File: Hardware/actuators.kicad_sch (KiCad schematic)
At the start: 10 parts, among them J11 Conn_01x08_Socket, J14 ServoCH1, J15 ServoCH2

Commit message: Finished Boosts and Sensors
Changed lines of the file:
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@@
 (kicad_sch
-	(version 20231120)
+	(version 20250114)
 	(generator "eeschema")
-	(generator_version "8.0")
+	(generator_version "9.0")
 	(paper "A4")
 	(junction
@@
 	(label "Servo2PWM"
 		(at 88.646 88.392 90)
-		(fields_autoplaced yes)
 		(effects
 			(font
@@
 	(label "Servo1PWM"
 		(at 96.7393 87.8116 90)
-		(fields_autoplaced yes)
 		(effects
 			(font
@@
 	(label "Servo1PWM"
 		(at 98.298 47.498 90)
-		(fields_autoplaced yes)
 		(effects
 			(font
@@
 	(label "Servo1PWM"
 		(at 64.516 94.234 180)
-		(fields_autoplaced yes)
 		(effects
 			(font
@@
 	(label "Servo2PWM"
 		(at 64.516 97.282 180)
-		(fields_autoplaced yes)
 		(effects
 			(font
@@
 	(label "Servo2PWM"
 		(at 98.298 62.738 90)
-		(fields_autoplaced yes)
 		(effects
 			(font
@@
 		(shape input)
 		(at 245.618 73.406 180)
-		(fields_autoplaced yes)
 		(effects
 			(font
@@
 		(shape bidirectional)
 		(at 67.056 94.234 0)
-		(fields_autoplaced yes)
 		(effects
 			(font
@@
 		(shape input)
 		(at 245.618 78.486 180)
-		(fields_autoplaced yes)
 		(effects
 			(font
@@
 		(shape input)
 		(at 215.646 107.95 180)
-		(fields_autoplaced yes)
 		(effects
 			(font
@@
 		(shape input)
 		(at 248.412 107.95 0)
-		(fields_autoplaced yes)
 		(effects
 			(font
@@
 		(shape input)
 		(at 245.618 75.946 180)
-		(fields_autoplaced yes)
 		(effects
 			(font
@@
 		(shape output)
 		(at 137.16 106.68 180)
-		(fields_autoplaced yes)
 		(effects
 			(font
@@
 		(shape input)
 		(at 245.618 70.866 180)
-		(fields_autoplaced yes)
 		(effects
 			(font
@@
 		(shape input)
 		(at 215.646 102.87 180)
-		(fields_autoplaced yes)
 		(effects
 			(font
@@
 		(shape input)
 		(at 248.412 105.41 0)
-		(fields_autoplaced yes)
 		(effects
 			(font
@@
 		(shape input)
 		(at 248.412 102.87 0)
-		(fields_autoplaced yes)
 		(effects
 			(font
@@
 		(shape bidirectional)
 		(at 67.056 97.282 0)
-		(fields_autoplaced yes)
 		(effects
 			(font
@@
 		(shape input)
 		(at 215.646 110.49 180)
-		(fields_autoplaced yes)
-		(effects
-			(font
+		(effects
+			(font

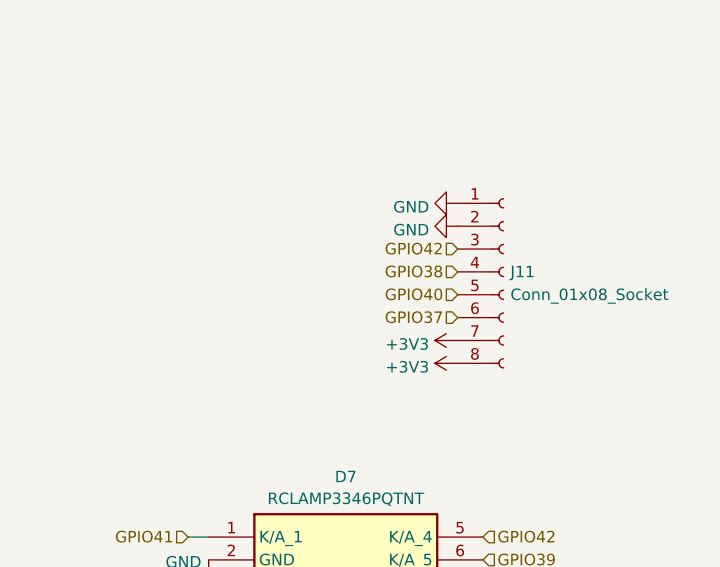
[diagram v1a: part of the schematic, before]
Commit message: Updated SD card, GPIOs, CAN, Power section
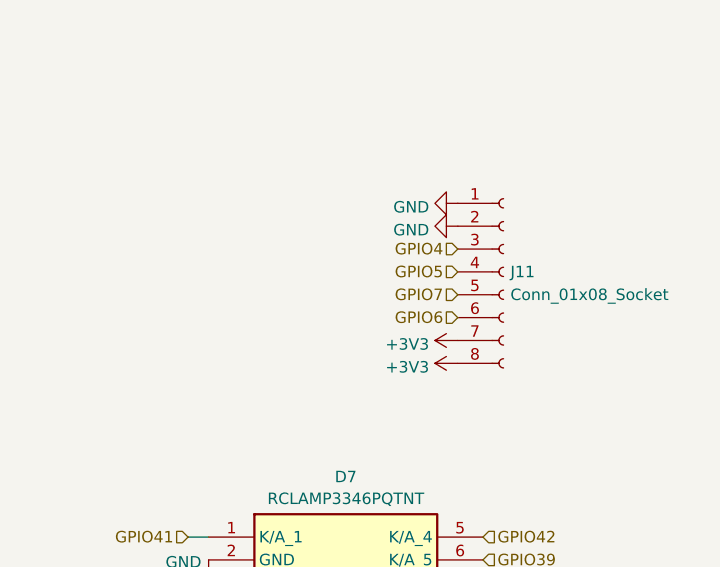
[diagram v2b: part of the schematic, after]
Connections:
- net GPIO37: no longer J11.6 (Pin_6)
- net GPIO38: no longer J11.4 (Pin_4)
- net GPIO40: no longer J11.5 (Pin_5)
- net GPIO42: no longer J11.3 (Pin_3)
- new net GPIO4: J11.3 (Pin_3)
- new net GPIO5: J11.4 (Pin_4)
- new net GPIO6: J11.6 (Pin_6)
- new net GPIO7: J11.5 (Pin_5)
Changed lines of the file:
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@@
 		)
 	)
-	(hierarchical_label "GPIO38"
+	(hierarchical_label "GPIO5"
 		(shape input)
 		(at 245.618 73.406 180)
@@
 		)
 	)
-	(hierarchical_label "GPIO37"
+	(hierarchical_label "GPIO7"
 		(shape input)
-		(at 245.618 78.486 180)
+		(at 245.618 75.946 180)
 		(effects
 			(font
@@
 		)
 	)
-	(hierarchical_label "GPIO40"
+	(hierarchical_label "GPIO6"
 		(shape input)
-		(at 245.618 75.946 180)
+		(at 245.618 78.486 180)
 		(effects
 			(font
@@
 		)
 	)
-	(hierarchical_label "GPIO42"
+	(hierarchical_label "GPIO4"
 		(shape input)
 		(at 245.618 70.866 180)

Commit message: Routed Switch and Servo driver subsystems
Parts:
- removed J11: Conn_01x08_Socket, Connector_PinSocket_2.54mm:PinSocket_2x04_P2.54mm_Vertical, symbol Connector:Conn_01x08_Socket
- added J5: Conn_01x04_Socket, Connector_PinHeader_2.54mm:PinHeader_1x04_P2.54mm_Vertical, symbol Connector:Conn_01x04_Socket
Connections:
- net GPIO41 is gone; now on net GPIO4: D7.1 (K/A_1)
- net GPIO42 is gone; now on net GPIO5: D7.5 (K/A_4)
- net +3V3: now also J5.4 (Pin_4)
- net GND: now also J5.1 (Pin_1)
- net GPIO4: now also J5.3 (Pin_3)
- net GPIO5: now also J5.2 (Pin_2)
- net GPIO37: no longer names the net of D7.4 (K/A_3)
- net GPIO38: no longer names the net of D7.3 (K/A_2)
- net GPIO39: no longer names the net of D7.6 (K/A_5)
- net GPIO40: no longer names the net of D7.7 (K/A_6)
- no-connect marks 0 -> 4
